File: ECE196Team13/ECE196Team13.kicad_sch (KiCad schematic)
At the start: 41 parts, among them M1 AO3401A, M2a1 AO3400A, M2b1 AO3400A, U1 CN3063, U2 MT3608, U3 SY6280AAC

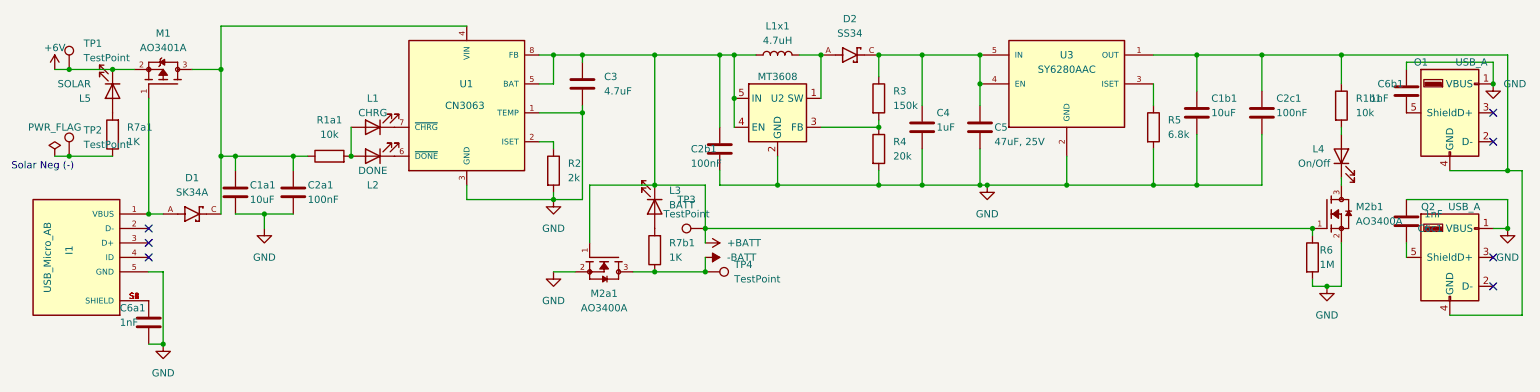
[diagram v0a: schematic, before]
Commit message: Updates to Solar Battery Stuff
New gerbers, new schematic kind-of (going to make it prettier later), new pcb design. MT3608 and Sy6280AAC layouts should be better.
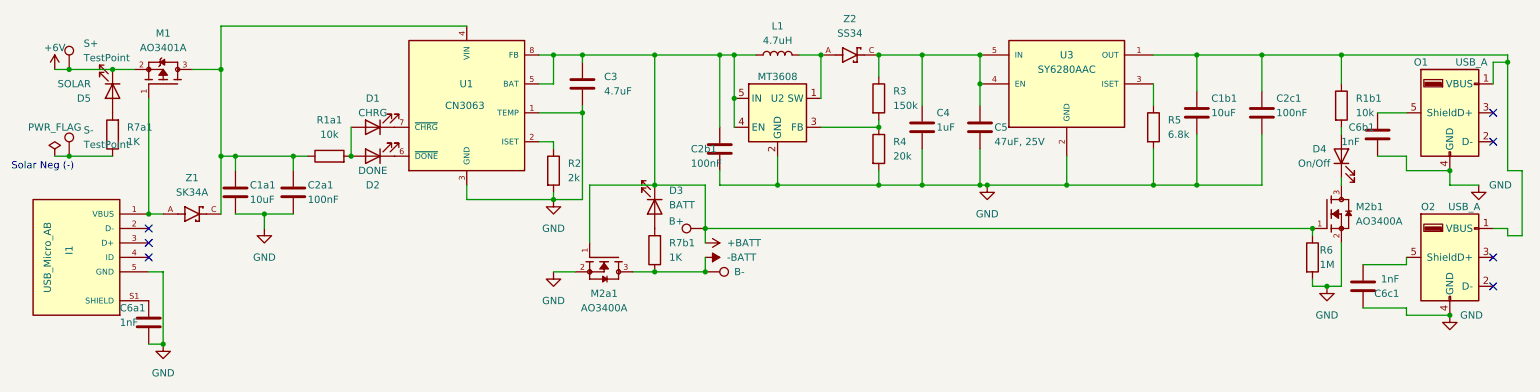
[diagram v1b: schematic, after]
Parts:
- O1, O2: footprint Connector_USB:USB_A_CNCTech_1001-011-01101_Horizontal -> Connector_USB:USB_A_CONNFLY_DS1095-WNR0
- R6: footprint R6:R0402 -> Resistor_SMD:R_0805_2012Metric
- renumbered TP3 to B+, TP4 to B-, L1 to D1, L2 to D2, L3 to D3, L4 to D4, L5 to D5, L1x1 to L1, TP1 to S+, TP2 to S-, D1 to Z1, D2 to Z2
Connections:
- net GND: now also C6b1.2, C6c1.1, O1.4 (GND), O2.4 (GND); no longer C6b1.1, C6c1.2, O1.1 (VBUS), O2.1 (VBUS)
- net at C1b1.1, C2c1.1, R1b1.1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: now also O1.1 (VBUS), O2.1 (VBUS); no longer O1.4 (GND), O2.4 (GND)
- net at O1.5 (Shield): now also C6b1.1; no longer C6b1.2
- net at O2.5 (Shield): now also C6c1.2; no longer C6c1.1
- new net: C6a1.1, I1.S1 (SHIELD)
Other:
- moved on the sheet: C6b1, C6c1
